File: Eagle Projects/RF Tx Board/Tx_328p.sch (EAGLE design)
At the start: 12 parts, among them U1 ATMEGA328P_TQFP

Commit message: GPS Code tweaks (tired to think :P)
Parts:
- removed SPI_HEADER: (no value), pinhead:PINHD-2X3
- added ISP1: AVRISP-BOX, adafruit:AVRISP-BOX
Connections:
- removed net N$4: SPI_HEADER.1
- removed net N$5: SPI_HEADER.3
- removed net N$6: SPI_HEADER.5
- new net RST: ISP1.RST
- net GND: now also ISP1.GND; no longer SPI_HEADER.6
- net MISO: now also ISP1.MISO
- net MOSI: now also ISP1.MOSI; no longer SPI_HEADER.4
- net SCK: now also ISP1.SCK
- net VCC: now also ISP1.VCC; no longer SPI_HEADER.2
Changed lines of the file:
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@@
 <setting verticaltext="up"/>
 </settings>
-<grid distance="0.1" unitdist="inch" unit="mm" style="lines" multiple="1" display="no" altdistance="0.01" altunitdist="inch" altunit="mm"/>
+<grid distance="0.1" unitdist="inch" unit="inch" style="lines" multiple="1" display="no" altdistance="0.01" altunitdist="inch" altunit="inch"/>
 <layers>
-<layer number="1" name="Top" color="4" fill="1" visible="yes" active="no"/>
-<layer number="16" name="Bottom" color="1" fill="1" visible="yes" active="no"/>
-<layer number="17" name="Pads" color="2" fill="1" visible="yes" active="no"/>
-<layer number="18" name="Vias" color="2" fill="1" visible="yes" active="no"/>
-<layer number="19" name="Unrouted" color="6" fill="1" visible="yes" active="no"/>
-<layer number="20" name="Dimension" color="15" fill="1" visible="yes" active="no"/>
-<layer number="21" name="tPlace" color="7" fill="1" visible="yes" active="no"/>
-<layer number="22" name="bPlace" color="7" fill="1" visible="yes" active="no"/>
-<layer number="23" name="tOrigins" color="15" fill="1" visible="yes" active="no"/>
-<layer number="24" name="bOrigins" color="15" fill="1" visible="yes" active="no"/>
-<layer number="25" name="tNames" color="7" fill="1" visible="yes" active="no"/>
-<layer number="26" name="bNames" color="7" fill="1" visible="yes" active="no"/>
-<layer number="27" name="tValues" color="7" fill="1" visible="yes" active="no"/>
-<layer number="28" name="bValues" color="7" fill="1" visible="yes" active="no"/>
+<layer number="1" name="Top" color="4" fill="1" visible="no" active="no"/>
+<layer number="16" name="Bottom" color="1" fill="1" visible="no" active="no"/>
+<layer number="17" name="Pads" color="2" fill="1" visible="no" active="no"/>
+<layer number="18" name="Vias" color="2" fill="1" visible="no" active="no"/>
+<layer number="19" name="Unrouted" color="6" fill="1" visible="no" active="no"/>
+<layer number="20" name="Dimension" color="15" fill="1" visible="no" active="no"/>
+<layer number="21" name="tPlace" color="7" fill="1" visible="no" active="no"/>
+<layer number="22" name="bPlace" color="7" fill="1" visible="no" active="no"/>
+<layer number="23" name="tOrigins" color="15" fill="1" visible="no" active="no"/>
+<layer number="24" name="bOrigins" color="15" fill="1" visible="no" active="no"/>
+<layer number="25" name="tNames" color="7" fill="1" visible="no" active="no"/>
+<layer number="26" name="bNames" color="7" fill="1" visible="no" active="no"/>
+<layer number="27" name="tValues" color="7" fill="1" visible="no" active="no"/>
+<layer number="28" name="bValues" color="7" fill="1" visible="no" active="no"/>
 <layer number="29" name="tStop" color="7" fill="3" visible="no" active="no"/>
 <layer number="30" name="bStop" color="7" fill="6" visible="no" active="no"/>
@@
 <layer number="35" name="tGlue" color="7" fill="4" visible="no" active="no"/>
 <layer number="36" name="bGlue" color="7" fill="5" visible="no" active="no"/>
-<layer number="37" name="tTest" color="7" fill="1" visible="yes" active="no"/>
-<layer number="38" name="bTest" color="7" fill="1" visible="yes" active="no"/>
+<layer number="37" name="tTest" color="7" fill="1" visible="no" active="no"/>
+<layer number="38" name="bTest" color="7" fill="1" visible="no" active="no"/>
 <layer number="39" name="tKeepout" color="4" fill="11" visible="no" active="no"/>
 <layer number="40" name="bKeepout" color="1" fill="11" visible="no" active="no"/>
@@
 <layer number="44" name="Drills" color="7" fill="1" visible="no" active="no"/>
 <layer number="45" name="Holes" color="7" fill="1" visible="no" active="no"/>
-<layer number="46" name="Milling" color="3" fill="1" visible="yes" active="no"/>
-<layer number="47" name="Measures" color="7" fill="1" visible="yes" active="no"/>
-<layer number="48" name="Document" color="7" fill="1" visible="yes" active="no"/>
-<layer number="49" name="Reference" color="7" fill="1" visible="yes" active="no"/>
-<layer number="50" name="dxf" color="7" fill="1" visible="yes" active="no"/>
-<layer number="51" name="tDocu" color="7" fill="1" visible="yes" active="no"/>
-<layer number="52" name="bDocu" color="7" fill="1" visible="yes" active="no"/>
-<layer number="53" name="tGND_GNDA" color="7" fill="9" visible="yes" active="no"/>
-<layer number="54" name="bGND_GNDA" color="1" fill="9" visible="yes" active="no"/>
-<layer number="56" name="wert" color="7" fill="1" visible="yes" active="no"/>
-<layer number="57" name="tCAD" color="7" fill="1" visible="yes" active="no"/>
-<layer number="59" name="tCarbon" color="7" fill="1" visible="yes" active="no"/>
-<layer number="60" name="bCarbon" color="7" fill="1" visible="yes" active="no"/>
+<layer number="46" name="Milling" color="3" fill="1" visible="no" active="no"/>
+<layer number="47" name="Measures" color="7" fill="1" visible="no" active="no"/>
+<layer number="48" name="Document" color="7" fill="1" visible="no" active="no"/>
+<layer number="49" name="Reference" color="7" fill="1" visible="no" active="no"/>
+<layer number="50" name="dxf" color="7" fill="1" visible="no" active="no"/>
+<layer number="51" name="tDocu" color="7" fill="1" visible="no" active="no"/>
+<layer number="52" name="bDocu" color="7" fill="1" visible="no" active="no"/>
+<layer number="53" name="tGND_GNDA" color="7" fill="9" visible="no" active="no"/>
+<layer number="54" name="bGND_GNDA" color="1" fill="9" visible="no" active="no"/>
+<layer number="56" name="wert" color="7" fill="1" visible="no" active="no"/>
+<layer number="57" name="tCAD" color="7" fill="1" visible="no" active="no"/>
+<layer number="59" name="tCarbon" color="7" fill="1" visible="no" active="no"/>
+<layer number="60" name="bCarbon" color="7" fill="1" visible="no" active="no"/>
 <layer number="90" name="Modules" color="5" fill="1" visible="yes" active="yes"/>
 <layer number="91" name="Nets" color="2" fill="1" visible="yes" active="yes"/>
@@
 <part name="GND1" library="supply1" deviceset="GND" device=""/>
 <part name="P+1" library="supply1" deviceset="VCC" device=""/>
-<part name="SPI_HEADER" library="pinhead" deviceset="PINHD-2X3" device=""/>
 <part name="P+2" library="supply1" deviceset="VCC" device=""/>
 <part name="GND2" library="supply1" deviceset="GND" device=""/>
@@
 <part name="P+7" library="supply1" deviceset="VCC" device=""/>
 <part name="GND7" library="supply1" deviceset="GND" device=""/>
+<part name="ISP1" library="adafruit" deviceset="AVRISP" device="-BOX"/>
 </parts>
 <sheets>
@@
 <instance part="GND1" gate="1" x="55.88" y="15.24"/>
 <instance part="P+1" gate="VCC" x="55.88" y="101.6"/>
-<instance part="SPI_HEADER" gate="A" x="187.96" y="35.56"/>
 <instance part="P+2" gate="VCC" x="203.2" y="48.26"/>
 <instance part="GND2" gate="1" x="203.2" y="17.78"/>
@@
 <instance part="P+7" gate="VCC" x="223.52" y="43.18"/>
 <instance part="GND7" gate="1" x="223.52" y="25.4"/>
+<instance part="ISP1" gate="G$1" x="180.34" y="35.56"/>
 </instances>
 <busses>
@@
 <pinref part="GND2" gate="1" pin="GND"/>
 <wire x1="203.2" y1="22.86" x2="203.2" y2="20.32" width="0.1524" layer="91"/>
-<pinref part="SPI_HEADER" gate="A" pin="6"/>
-<wire x1="193.04" y1="33.02" x2="203.2" y2="33.02" width="0.1524" layer="91"/>
 <wire x1="203.2" y1="33.02" x2="203.2" y2="20.32" width="0.1524" layer="91"/>
+<pinref part="ISP1" gate="G$1" pin="GND"/>
+<wire x1="203.2" y1="33.02" x2="195.58" y2="33.02" width="0.1524" layer="91"/>
 </segment>
 <segment>
@@
 </segment>
 <segment>
-<pinref part="SPI_HEADER" gate="A" pin="2"/>
 <pinref part="P+2" gate="VCC" pin="VCC"/>
-<wire x1="193.04" y1="38.1" x2="203.2" y2="38.1" width="0.1524" layer="91"/>
 <wire x1="203.2" y1="38.1" x2="203.2" y2="45.72" width="0.1524" layer="91"/>
+<pinref part="ISP1" gate="G$1" pin="VCC"/>
+<wire x1="195.58" y1="38.1" x2="203.2" y2="38.1" width="0.1524" layer="91"/>
 </segment>
 </net>
@@
 </segment>
 <segment>
-<pinref part="SPI_HEADER" gate="A" pin="4"/>
-<wire x1="193.04" y1="35.56" x2="208.28" y2="35.56" width="0.1524" layer="91"/>
-<label x="210.82" y="35.56" size="1.778" layer="95"/>
+<pinref part="ISP1" gate="G$1" pin="MOSI"/>
+<wire x1="195.58" y1="35.56" x2="203.2" y2="35.56" width="0.1524" layer="91"/>
+<label x="203.2" y="35.56" size="1.778" layer="95"/>
 </segment>
 </net>
@@
 <label x="132.08" y="35.56" size="1.778" layer="95"/>
 </segment>
+<segment>
+<pinref part="ISP1" gate="G$1" pin="MISO"/>
+<wire x1="167.64" y1="38.1" x2="162.56" y2="38.1" width="0.1524" layer="91"/>
+<label x="154.94" y="38.1" size="1.778" layer="95"/>
+</segment>
 </net>
 <net name="SCK" class="0">
@@
 <label x="132.08" y="33.02" size="1.778" layer="95"/>
 </segment>
-</net>
-<net name="N$4" class="0">
-<segment>
-<pinref part="SPI_HEADER" gate="A" pin="1"/>
-<wire x1="185.42" y1="38.1" x2="177.8" y2="38.1" width="0.1524" layer="91"/>
-</segment>
-</net>
-<net name="N$5" class="0">
-<segment>
-<pinref part="SPI_HEADER" gate="A" pin="3"/>
-<wire x1="185.42" y1="35.56" x2="177.8" y2="35.56" width="0.1524" layer="91"/>
-</segment>
-</net>
-<net name="N$6" class="0">
-<segment>
-<pinref part="SPI_HEADER" gate="A" pin="5"/>
-<wire x1="185.42" y1="33.02" x2="177.8" y2="33.02" width="0.1524" layer="91"/>
-</segment>
-</net>
+<segment>
+<pinref part="ISP1" gate="G$1" pin="SCK"/>
+<wire x1="167.64" y1="35.56" x2="162.56" y2="35.56" width="0.1524" layer="91"/>
+<label x="154.94" y="35.56" size="1.778" layer="95"/>
+</segment>
+</net>
+<net name="RST" class="0">
+<segment>
+<pinref part="ISP1" gate="G$1" pin="RST"/>
+<wire x1="167.64" y1="33.02" x2="162.56" y2="33.02" width="0.1524" layer="91"/>
+<label x="154.94" y="33.02" size="1.778" layer="95"/>
+</segment>
+</net>

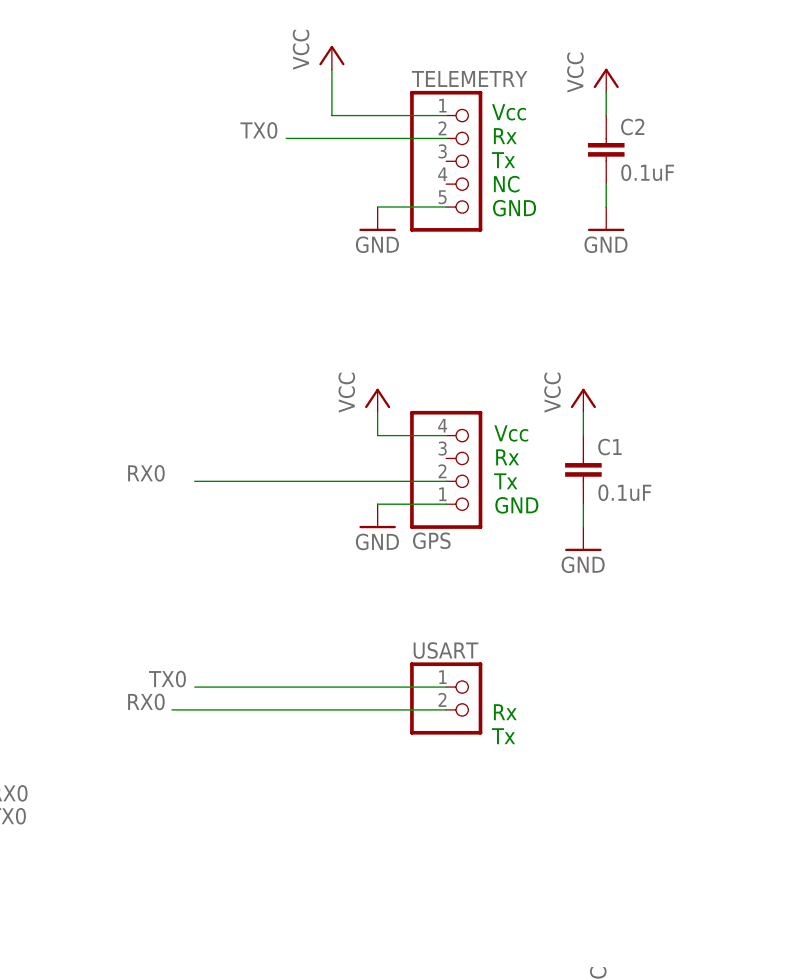
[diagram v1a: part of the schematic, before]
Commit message: Added Tx/Rx LEDs for board + measurements of GPS & RF boards for comparison *cough*Autorouted *cough* and still broken, redoing manually :P
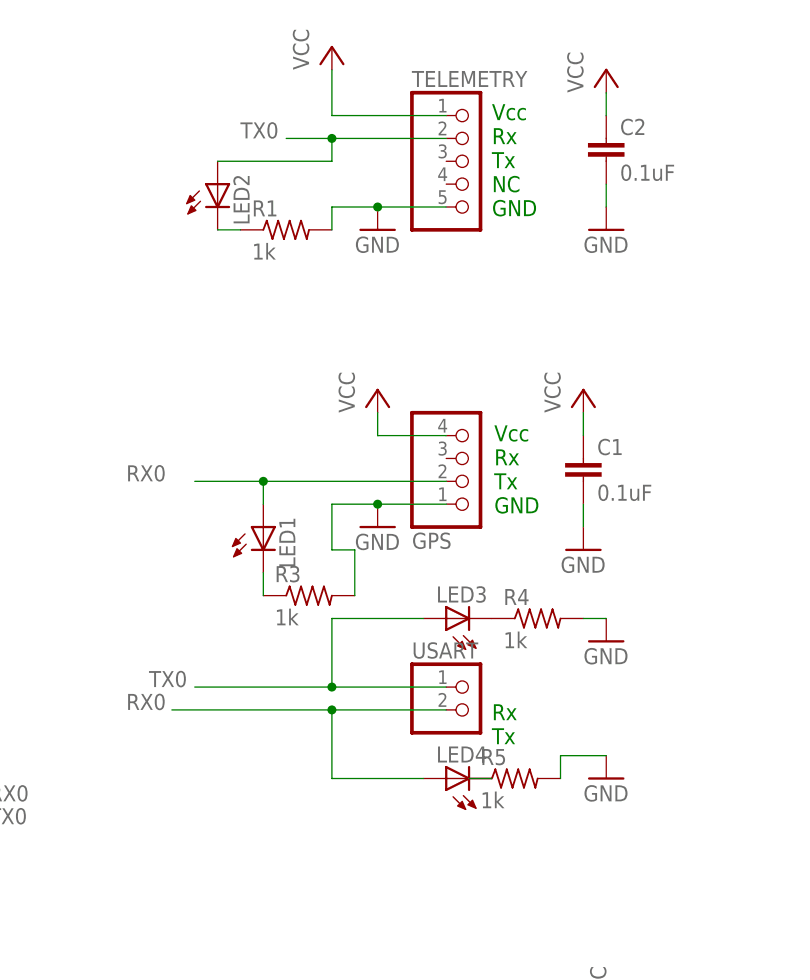
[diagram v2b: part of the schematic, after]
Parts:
- added LED1, LED2, LED3, LED4: (no value), led:LEDCHIP-LED0805
- added R1, R3, R4, R5: 1k, rcl:R-US_M0805
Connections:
- new net N$4: LED1.C, R3.1
- new net N$5: LED2.C, R1.1
- new net N$6: LED3.C, R4.1
- new net N$8: LED4.C, R5.1
- net GND: now also R1.2, R3.2, R4.2, R5.2
- net RX0: now also LED1.A, LED4.A
- net TX0: now also LED2.A, LED3.A
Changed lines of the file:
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@@
 <part name="GND7" library="supply1" deviceset="GND" device=""/>
 <part name="ISP1" library="adafruit" deviceset="AVRISP" device="-BOX"/>
+<part name="LED1" library="led" deviceset="LED" device="CHIP-LED0805"/>
+<part name="LED2" library="led" deviceset="LED" device="CHIP-LED0805"/>
+<part name="R1" library="rcl" deviceset="R-US_" device="M0805" value="1k"/>
+<part name="R3" library="rcl" deviceset="R-US_" device="M0805" value="1k"/>
+<part name="GND8" library="supply1" deviceset="GND" device=""/>
+<part name="GND9" library="supply1" deviceset="GND" device=""/>
+<part name="LED3" library="led" deviceset="LED" device="CHIP-LED0805"/>
+<part name="LED4" library="led" deviceset="LED" device="CHIP-LED0805"/>
+<part name="R4" library="rcl" deviceset="R-US_" device="M0805" value="1k"/>
+<part name="R5" library="rcl" deviceset="R-US_" device="M0805" value="1k"/>
 </parts>
 <sheets>
@@
 <instance part="GND7" gate="1" x="223.52" y="25.4"/>
 <instance part="ISP1" gate="G$1" x="180.34" y="35.56"/>
+<instance part="LED1" gate="G$1" x="162.56" y="99.06"/>
+<instance part="LED2" gate="G$1" x="157.48" y="137.16"/>
+<instance part="R1" gate="G$1" x="165.1" y="132.08"/>
+<instance part="R3" gate="G$1" x="167.64" y="91.44"/>
+<instance part="GND8" gate="1" x="200.66" y="71.12"/>
+<instance part="GND9" gate="1" x="200.66" y="86.36"/>
+<instance part="LED3" gate="G$1" x="182.88" y="88.9" rot="R90"/>
+<instance part="LED4" gate="G$1" x="182.88" y="71.12" rot="R90"/>
+<instance part="R4" gate="G$1" x="193.04" y="88.9"/>
+<instance part="R5" gate="G$1" x="190.5" y="71.12"/>
 </instances>
 <busses>
@@
 <pinref part="GND3" gate="1" pin="GND"/>
 <wire x1="182.88" y1="101.6" x2="175.26" y2="101.6" width="0.1524" layer="91"/>
+<pinref part="R3" gate="G$1" pin="2"/>
+<wire x1="172.72" y1="91.44" x2="172.72" y2="96.52" width="0.1524" layer="91"/>
+<wire x1="172.72" y1="96.52" x2="170.18" y2="96.52" width="0.1524" layer="91"/>
+<wire x1="170.18" y1="96.52" x2="170.18" y2="101.6" width="0.1524" layer="91"/>
+<wire x1="170.18" y1="101.6" x2="175.26" y2="101.6" width="0.1524" layer="91"/>
+<junction x="175.26" y="101.6"/>
 </segment>
 <segment>
@@
 <wire x1="182.88" y1="134.62" x2="175.26" y2="134.62" width="0.1524" layer="91"/>
 <pinref part="GND4" gate="1" pin="GND"/>
+<wire x1="170.18" y1="132.08" x2="170.18" y2="134.62" width="0.1524" layer="91"/>
+<wire x1="170.18" y1="134.62" x2="175.26" y2="134.62" width="0.1524" layer="91"/>
+<junction x="175.26" y="134.62"/>
+<pinref part="R1" gate="G$1" pin="2"/>
 </segment>
 <segment>
@@
 <pinref part="C5" gate="G$1" pin="2"/>
 <wire x1="223.52" y1="27.94" x2="223.52" y2="30.48" width="0.1524" layer="91"/>
+</segment>
+<segment>
+<pinref part="GND9" gate="1" pin="GND"/>
+<pinref part="R4" gate="G$1" pin="2"/>
+<wire x1="200.66" y1="88.9" x2="198.12" y2="88.9" width="0.1524" layer="91"/>
+</segment>
+<segment>
+<pinref part="R5" gate="G$1" pin="2"/>
+<wire x1="195.58" y1="71.12" x2="195.58" y2="73.66" width="0.1524" layer="91"/>
+<pinref part="GND8" gate="1" pin="GND"/>
+<wire x1="195.58" y1="73.66" x2="200.66" y2="73.66" width="0.1524" layer="91"/>
 </segment>
 </net>
@@
 <segment>
 <pinref part="USART" gate="G$1" pin="1"/>
-<wire x1="182.88" y1="81.28" x2="154.94" y2="81.28" width="0.1524" layer="91"/>
+<wire x1="182.88" y1="81.28" x2="170.18" y2="81.28" width="0.1524" layer="91"/>
 <label x="149.86" y="81.28" size="1.778" layer="95"/>
+<junction x="170.18" y="81.28"/>
+<wire x1="170.18" y1="81.28" x2="154.94" y2="81.28" width="0.1524" layer="91"/>
+<pinref part="LED3" gate="G$1" pin="A"/>
+<wire x1="180.34" y1="88.9" x2="170.18" y2="88.9" width="0.1524" layer="91"/>
+<wire x1="170.18" y1="88.9" x2="170.18" y2="81.28" width="0.1524" layer="91"/>
 </segment>
 <segment>
 <pinref part="TELEMETRY" gate="A" pin="2"/>
-<wire x1="182.88" y1="142.24" x2="165.1" y2="142.24" width="0.1524" layer="91"/>
+<wire x1="182.88" y1="142.24" x2="170.18" y2="142.24" width="0.1524" layer="91"/>
 <label x="160.02" y="142.24" size="1.778" layer="95"/>
+<junction x="170.18" y="142.24"/>
+<wire x1="170.18" y1="142.24" x2="165.1" y2="142.24" width="0.1524" layer="91"/>
+<wire x1="170.18" y1="142.24" x2="170.18" y2="139.7" width="0.1524" layer="91"/>
+<pinref part="LED2" gate="G$1" pin="A"/>
+<wire x1="170.18" y1="139.7" x2="157.48" y2="139.7" width="0.1524" layer="91"/>
 </segment>
 </net>
@@
 <segment>
 <pinref part="USART" gate="G$1" pin="2"/>
-<wire x1="182.88" y1="78.74" x2="152.4" y2="78.74" width="0.1524" layer="91"/>
+<wire x1="182.88" y1="78.74" x2="170.18" y2="78.74" width="0.1524" layer="91"/>
 <label x="147.32" y="78.74" size="1.778" layer="95"/>
+<junction x="170.18" y="78.74"/>
+<wire x1="170.18" y1="78.74" x2="152.4" y2="78.74" width="0.1524" layer="91"/>
+<wire x1="170.18" y1="78.74" x2="170.18" y2="71.12" width="0.1524" layer="91"/>
+<pinref part="LED4" gate="G$1" pin="A"/>
+<wire x1="170.18" y1="71.12" x2="180.34" y2="71.12" width="0.1524" layer="91"/>
 </segment>
 <segment>
 <pinref part="GPS" gate="A" pin="2"/>
-<wire x1="154.94" y1="104.14" x2="182.88" y2="104.14" width="0.1524" layer="91"/>
+<wire x1="154.94" y1="104.14" x2="162.56" y2="104.14" width="0.1524" layer="91"/>
 <label x="147.32" y="104.14" size="1.778" layer="95"/>
+<junction x="162.56" y="104.14"/>
+<wire x1="162.56" y1="104.14" x2="182.88" y2="104.14" width="0.1524" layer="91"/>
+<pinref part="LED1" gate="G$1" pin="A"/>
+<wire x1="162.56" y1="104.14" x2="162.56" y2="101.6" width="0.1524" layer="91"/>
 </segment>
 </net>
@@
 </segment>
 </net>
+<net name="N$5" class="0">
+<segment>
+<pinref part="R1" gate="G$1" pin="1"/>
+<pinref part="LED2" gate="G$1" pin="C"/>
+<wire x1="157.48" y1="132.08" x2="160.02" y2="132.08" width="0.1524" layer="91"/>
+</segment>
+</net>
+<net name="N$4" class="0">
+<segment>
+<pinref part="LED1" gate="G$1" pin="C"/>
+<pinref part="R3" gate="G$1" pin="1"/>
+<wire x1="162.56" y1="93.98" x2="162.56" y2="91.44" width="0.1524" layer="91"/>
+</segment>
+</net>
+<net name="N$6" class="0">
+<segment>
+<pinref part="LED3" gate="G$1" pin="C"/>
+<pinref part="R4" gate="G$1" pin="1"/>
+</segment>
+</net>
+<net name="N$8" class="0">
+<segment>
+<pinref part="LED4" gate="G$1" pin="C"/>
+<pinref part="R5" gate="G$1" pin="1"/>
+<wire x1="185.42" y1="71.12" x2="187.96" y2="71.12" width="0.1524" layer="91"/>
+</segment>
+</net>

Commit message: Misc board tweaks
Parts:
- added ..2: 1k, rcl:R-US_M0805
- added PWR_LED: (no value), led:LEDCHIP-LED0805
- added RESET: TAC_SWITCHSMD, SparkFun-Retired:TAC_SWITCHSMD
- added S1: SKHMPSE010, switch:SKHMPSE010
- C1, C2, C4, C5: device resistor:C-EUC0805K -> resistor:C-USC0805
- renumbered LED1 to TX_LED_GPS, LED2 to RX_3DR_LED, LED3 to RX_LED, LED4 to TX_LED, R4 to .., R5 to .
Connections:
- new net N$7: ..2.1, PWR_LED.A
- net GND: now also PWR_LED.C, RESET.1, RESET.2, S1.1.1, S1.1.2
- net VCC: now also ..2.2, RESET.3, RESET.4, S1.2.1, S1.2.2
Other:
- note added: "ICSP / SPI Programming header"

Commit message: More Board Edits *Imported Ben's CAN PCB layout *Revised schematic for neatness *Added pinheaders as spec'd for SMPS module
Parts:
- added C3, C6: 22pF, resistor:C-EUC0805K
- added C7, C8: 100nF, resistor:C-EUC0805K
- added GND, GND_2, VCC, VIN: (no value), pinhead:PINHD-1X1
- added LED1: RX, led:LEDCHIP-LED0805
- added LED2: TX, led:LEDCHIP-LED0805
- added LED3: INT, led:LEDCHIP-LED0805
- added Q3: 16MHz, crystal:CRYSTALHC49S
- added Q4: 16MHz, crystal:CRYSTALHC49UP
- added R4, R5, R6: 1k, resistor:R-US_R0805
- added R7, R8: 100k, resistor:R-US_R0805
- added U$1: MCP2515SO, RobThePyro:MCP2515SO
- added U2: MCP2551, SparkFun:MCP2551
- added Z1, Z2: TVS-UD-SOD323, supressor:TVS-UD-SOD323
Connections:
- new net +5V: C7.2, C8.2, R4.2, R5.2, R6.2, R7.1, U$1G$2.VDD, U2.VDD
- new net CANCS: U$1G$1.!CS
- new net CANH: U2.CANH, Z1.C
- new net CANINT: LED3.C, U$1G$1.!INT
- new net CANL: U2.CANL, Z2.C
- new net CANRST: R7.2, U$1G$1.!RESET
- new net CANSTBY: R8.1, U2.RS
- new net N$10: LED1.A, R4.1
- new net N$11: LED2.A, R5.1
- new net N$12: LED3.A, R6.1
- new net N$13: C3.1, Q3.2, Q4.2, U$1G$1.OSC1
- new net N$14: C6.1, Q3.1, Q4.1, U$1G$1.OSC2
- new net RXCAN: LED1.C, U$1G$1.RXCAN, U2.RXD
- new net TXCAN: LED2.C, U$1G$1.TXCAN, U2.TXD
- net GND: now also C3.2, C6.2, C7.1, C8.1, GND.1, GND_2.1, R8.2, U$1G$2.VSS, U2.VSS, Z1.A, Z2.A
- net MISO: now also U$1G$1.SO
- net MOSI: now also U$1G$1.SI
- net SCK: now also U$1G$1.SCK
- net VCC: now also VCC.1
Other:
- note added: "CAN Interface"
- note added: "GPS USART Connection & UART Extra pins"
- note added: "ICSP Header"
- note added: "Pins for SMPS board"
- note added: "Reset Switch & Power LED"
- note added: "Solar EV TX Board and Logic"
- note added: "Telemetry USART Connection"
